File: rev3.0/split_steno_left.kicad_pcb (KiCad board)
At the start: 2 copper layers, 99.7 x 74.2 mm, 44 parts, among them J1 USB_B, J2 Audio-Jack-4, J3 Conn_02x04_Odd_Even, J4 Conn_01x03, J5 Conn_01x03, J6 Conn_01x02, M2 MountingHole_2.2mm_M2, P1 TC2030-IDC, SW1 SW_Push, SW10 SW_Push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

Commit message: library managed
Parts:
- C1, C2, C3, C4, C5: footprint Capacitors_SMD:C_0603_HandSoldering -> lib_fp:C_0603_HandSoldering
- F1: footprint Fuse_Holders_and_Fuses:Fuse_SMD1206_HandSoldering -> lib_fp:Fuse_SMD1206_HandSoldering
- J1: footprint keyboard_parts:USB_miniB_hirose_5S8 -> lib_fp:USB_miniB_hirose_5S8
- J2: footprint Keebio-Parts:TRRS-PJ-320A -> lib_fp:TRRS-PJ-320A
- J3: footprint Pin_Headers:Pin_Header_Straight_2x04_Pitch2.54mm -> lib_fp:Pin_Header_Straight_2x04_Pitch2.54mm
- J4, J5: footprint Pin_Headers:Pin_Header_Straight_1x03_Pitch2.54mm -> lib_fp:Pin_Header_Straight_1x03_Pitch2.54mm
- J6: footprint Pin_Headers:Pin_Header_Straight_1x02_Pitch2.54mm -> lib_fp:Pin_Header_Straight_1x02_Pitch2.54mm
- P1: footprint Tag-Connect:TC2030-NL_SMALL_AND_IDC_PDI -> lib_fp:TC2030-NL_SMALL_AND_IDC_PDI
- R1, R2: footprint Resistors_SMD:R_0603_HandSoldering -> lib_fp:R_0603_HandSoldering
- SW1, SW10, SW11, SW12, SW13, SW14, SW15, SW16, SW17, SW18, SW2, SW3, SW4, SW5, SW6, SW7, SW8, SW9: footprint MX_Alps_Hybrid:MX-1U-NoLED -> lib_fp:MX-1U-NoLED
- SW19, SW20: footprint MX_Alps_Hybrid:MX-2U-NoLED -> lib_fp:MX-2U-NoLED
- U1: footprint TO_SOT_Packages_SMD:SOT-23-5_HandSoldering -> lib_fp:SOT-23-5_HandSoldering
- U2: footprint Housings_QFP:TQFP-44_10x10mm_Pitch0.8mm -> lib_fp:TQFP-44_10x10mm_Pitch0.8mm

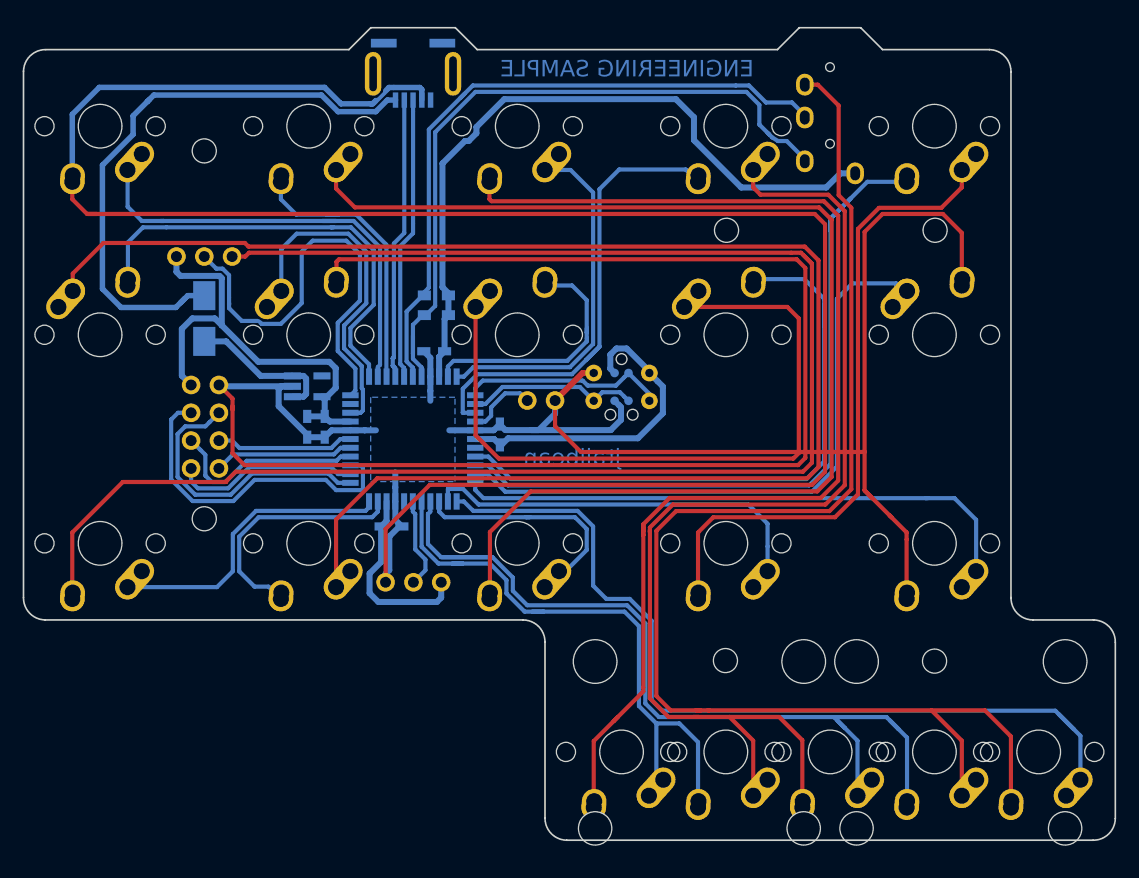
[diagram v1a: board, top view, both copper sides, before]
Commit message: filled gnd plane on left
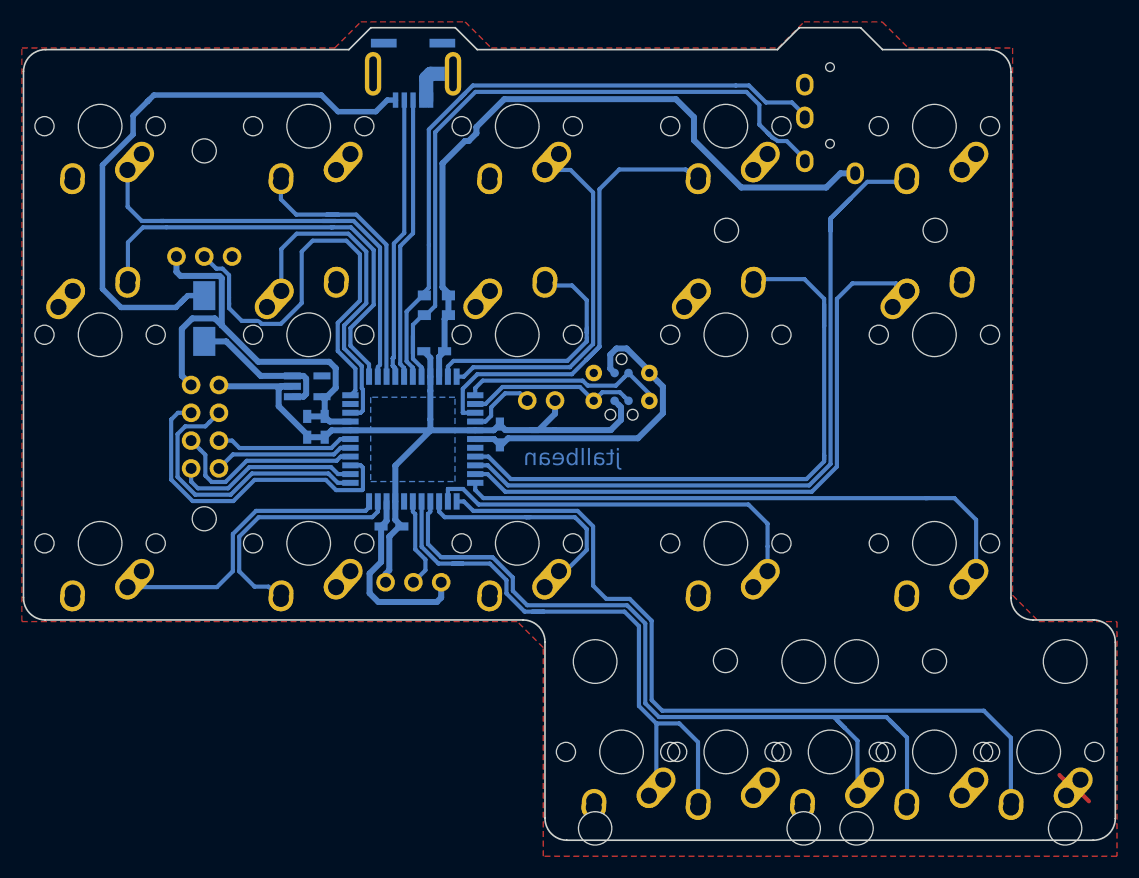
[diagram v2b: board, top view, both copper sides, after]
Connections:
- J1 pad 5: Net-(J1-Pad5) -> GND
- J1 pad 6: (no net) -> GND
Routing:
- net GND: track 1315.3 -> 82.1 mm
- net /KEY18: track 79.2 -> 73.4 mm
- added copper zone on F.Cu, net GND
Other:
- board text removed: "ENGINEERING SAMPLE"

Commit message: finished right hand
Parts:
- G***: footprint airi_logo:airi_icon-7.6 -> lib_fp:airi_icon-7.6
- M2 (x6): footprint Mounting_Holes:MountingHole_2.2mm_M2 -> lib_fp:MountingHole_2.2mm_M2
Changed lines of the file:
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@@
     (add_net VCC)
   )
-  (module airi_logo:airi_icon-7.6 (layer B.Cu)
+  (module lib_fp:airi_icon-7.6 (layer B.Cu)
     (at 80.93 73.84 180)
     (fp_text reference G*** (at 0 0 180) (layer B.SilkS) hide
@@
       (xy 1.69672 -0.335006) (xy 1.69672 -1.69672)) (layer B.Mask) (width 0.01))
   )
-  (module Mounting_Holes:MountingHole_2.2mm_M2 locked (layer F.Cu)
+  (module lib_fp:MountingHole_2.2mm_M2 locked (layer F.Cu)
     (at 128.6 94.1)
     (descr "Mounting Hole 2.2mm, no annular, M2")
@@
     (pad 1 np_thru_hole circle (at 0 0) (size 2.2 2.2) (drill 2.2) (layers *.Cu *.Mask))
   )
-  (module Mounting_Holes:MountingHole_2.2mm_M2 locked (layer F.Cu)
+  (module lib_fp:MountingHole_2.2mm_M2 locked (layer F.Cu)
     (at 109.5 94.05)
     (descr "Mounting Hole 2.2mm, no annular, M2")
@@
     (pad 1 np_thru_hole circle (at 0 0) (size 2.2 2.2) (drill 2.2) (layers *.Cu *.Mask))
   )
-  (module Mounting_Holes:MountingHole_2.2mm_M2 locked (layer F.Cu)
+  (module lib_fp:MountingHole_2.2mm_M2 locked (layer F.Cu)
     (at 128.65 54.75)
     (descr "Mounting Hole 2.2mm, no annular, M2")
@@
     (pad 1 np_thru_hole circle (at 0 0) (size 2.2 2.2) (drill 2.2) (layers *.Cu *.Mask))
   )
-  (module Mounting_Holes:MountingHole_2.2mm_M2 locked (layer F.Cu)
+  (module lib_fp:MountingHole_2.2mm_M2 locked (layer F.Cu)
     (at 109.6 54.75)
     (descr "Mounting Hole 2.2mm, no annular, M2")
@@
     (pad 1 np_thru_hole circle (at 0 0) (size 2.2 2.2) (drill 2.2) (layers *.Cu *.Mask))
   )
-  (module Mounting_Holes:MountingHole_2.2mm_M2 locked (layer F.Cu)
+  (module lib_fp:MountingHole_2.2mm_M2 locked (layer F.Cu)
     (at 61.9 81.1)
     (descr "Mounting Hole 2.2mm, no annular, M2")
@@
     (pad 1 np_thru_hole circle (at 0 0) (size 2.2 2.2) (drill 2.2) (layers *.Cu *.Mask))
   )
-  (module Mounting_Holes:MountingHole_2.2mm_M2 locked (layer F.Cu)
+  (module lib_fp:MountingHole_2.2mm_M2 locked (layer F.Cu)
     (at 61.9 47.5)
     (descr "Mounting Hole 2.2mm, no annular, M2")
